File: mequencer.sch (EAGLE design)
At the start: 69 parts, among them IC1 NE555D, IC10 LF353D, IC11 NE555D, IC12 NE555D, IC2 4163D, IC3 74HC85D, IC4 4051D, IC5 4051D, IC6 74HCT04D, IC7 4051D, IC8 4051D, IC9 LF353D, U1 74LVC1G08SE-7

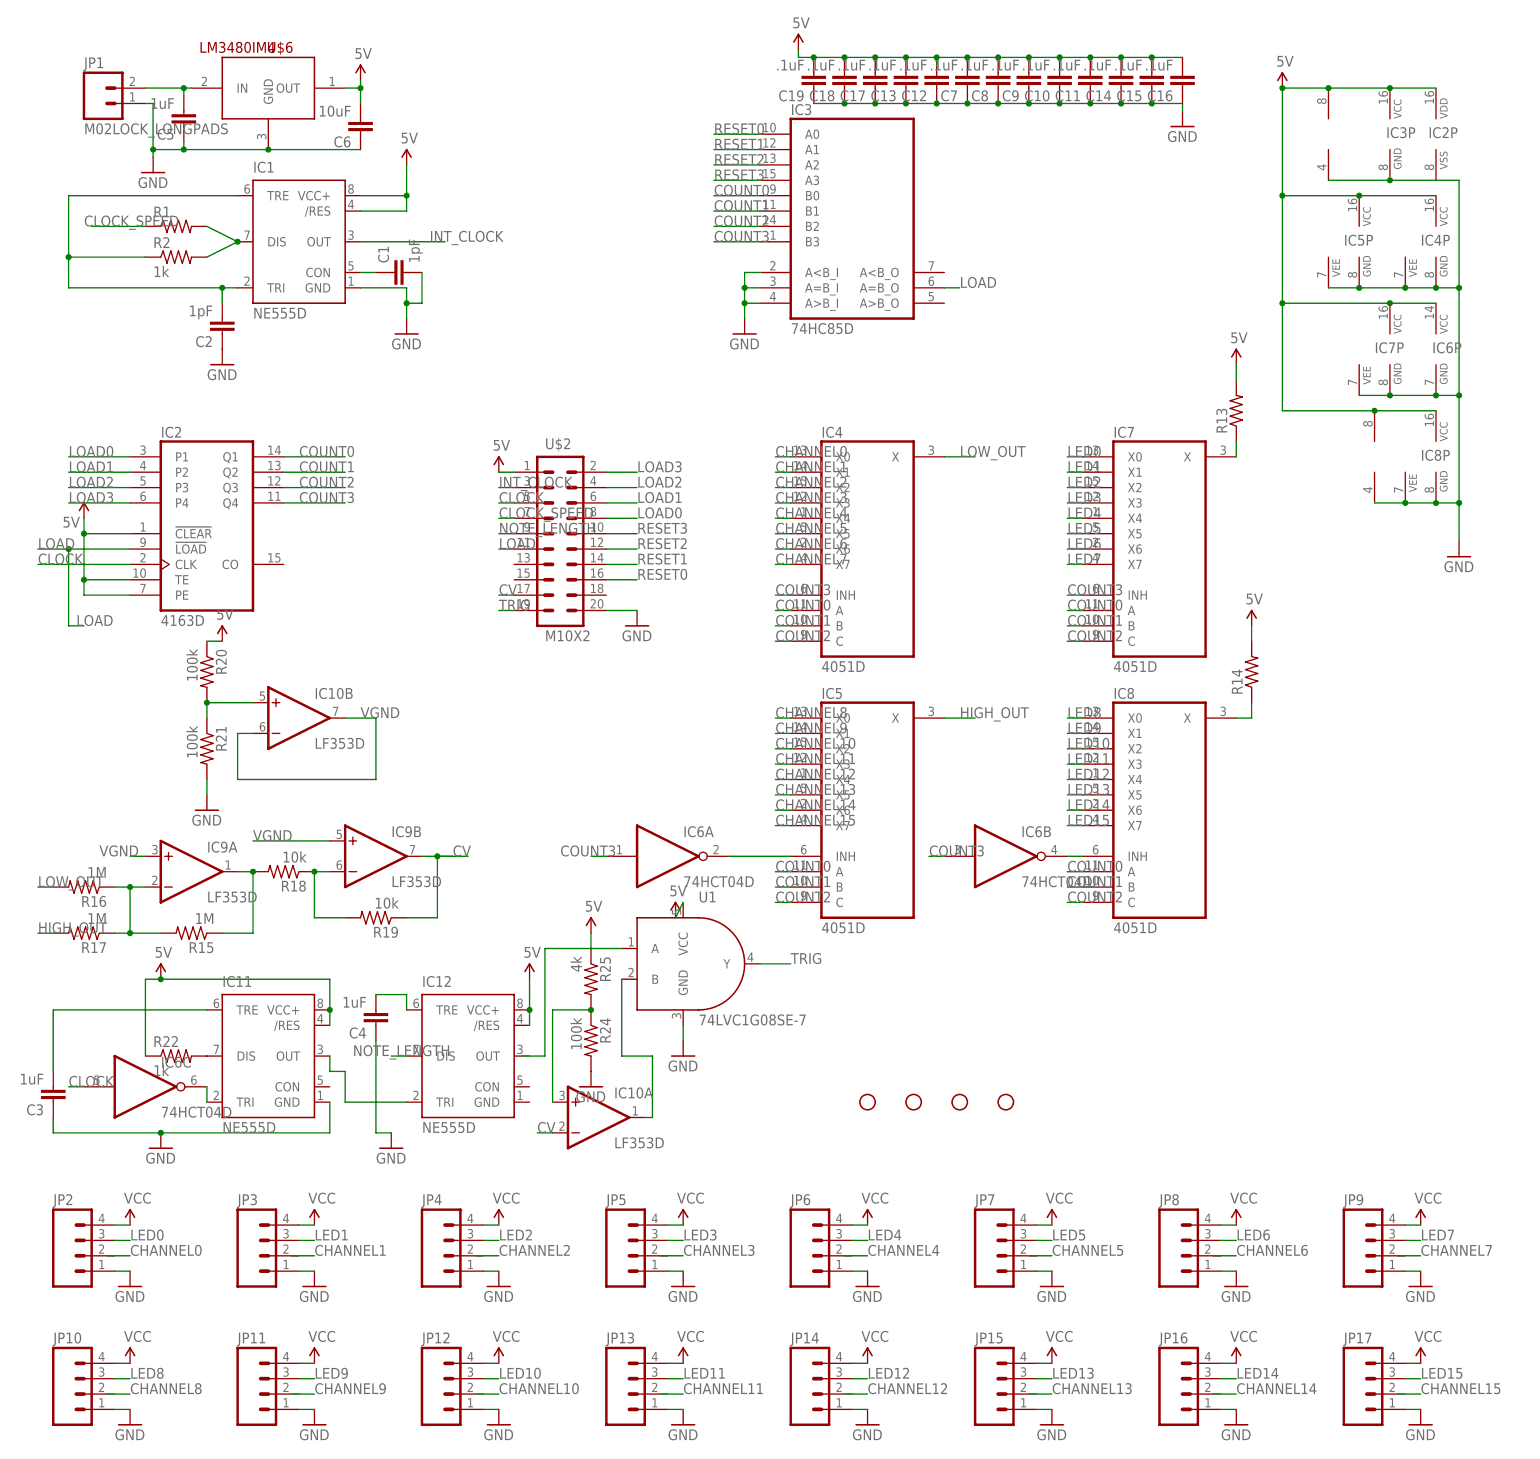
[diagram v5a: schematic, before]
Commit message: test points and jack resistors
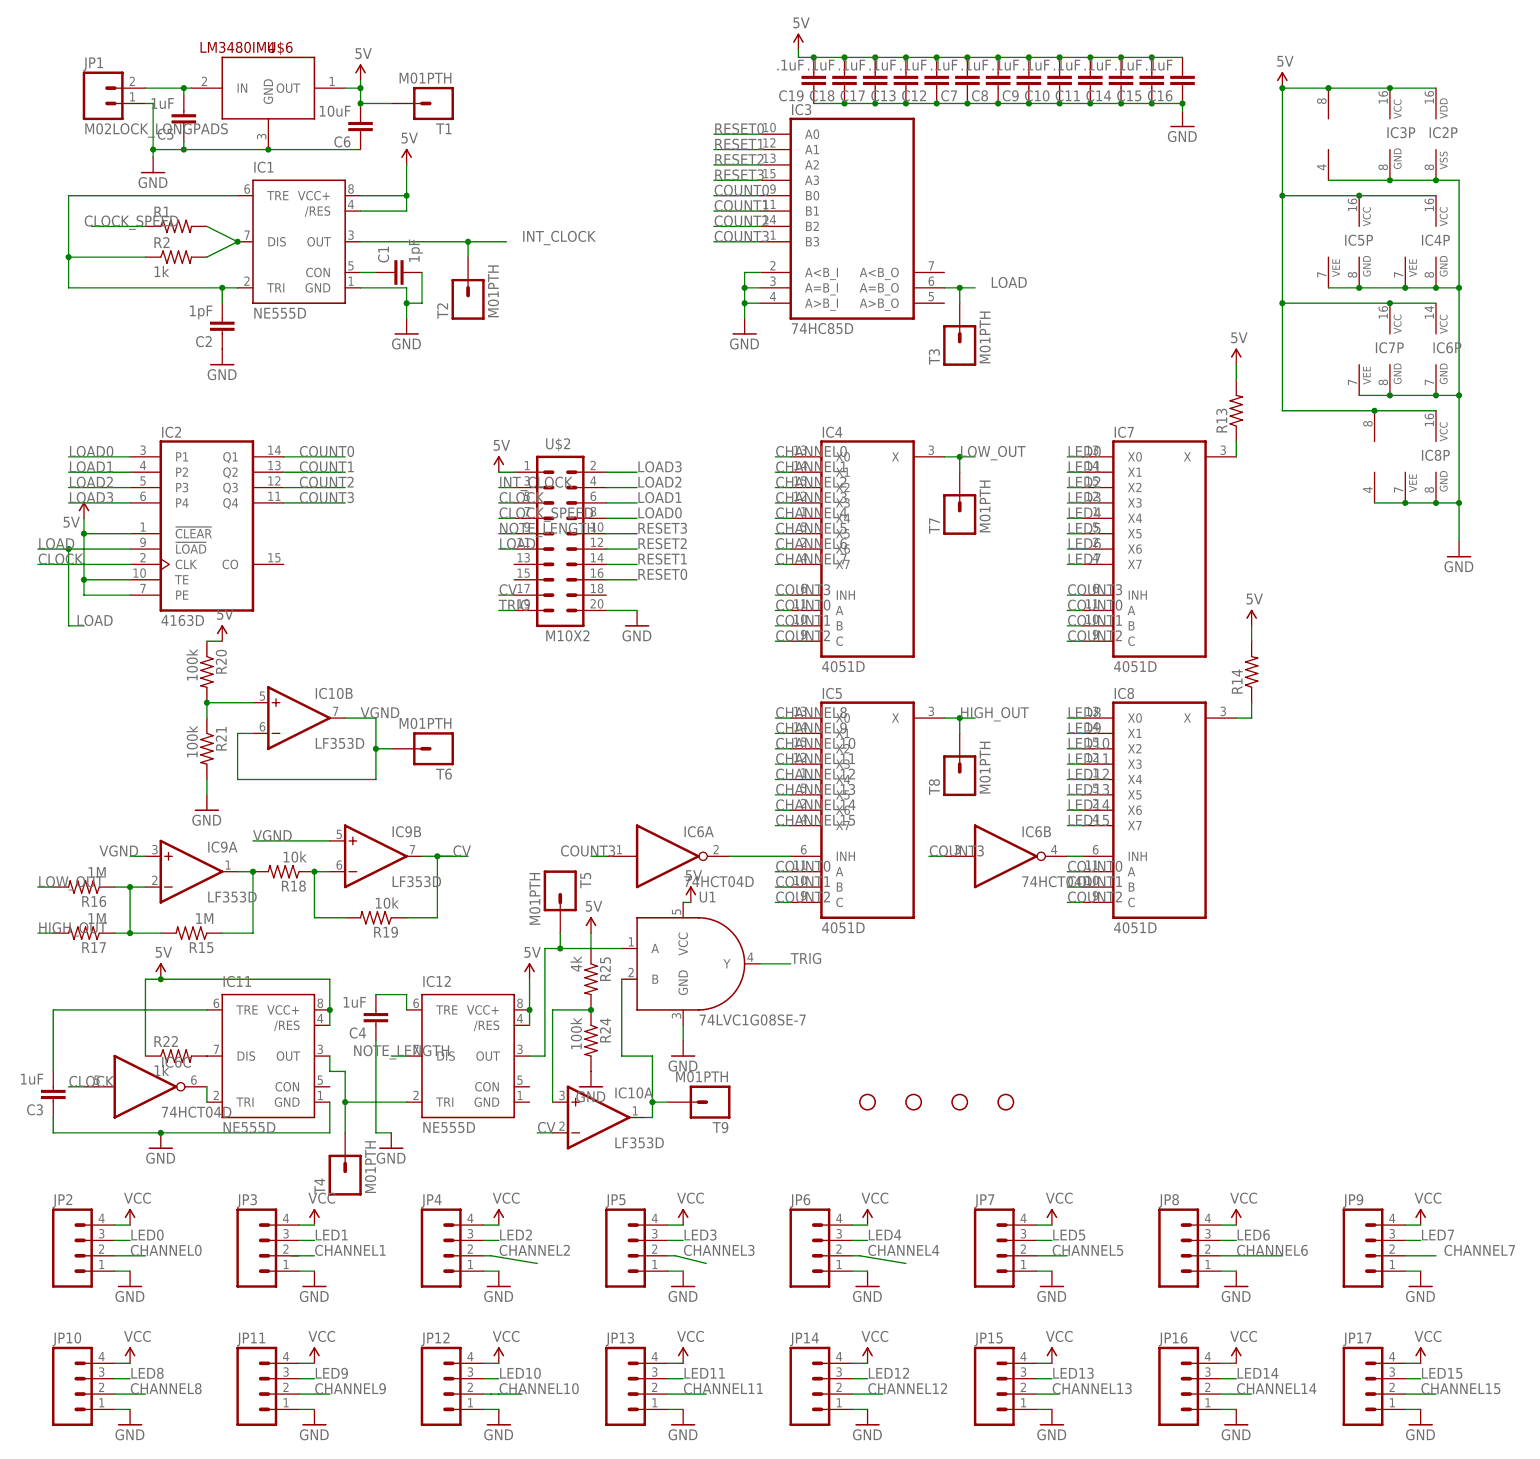
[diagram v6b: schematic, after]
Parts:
- added T1, T2, T3, T4, T5, T6, T7, T8, T9: M01PTH, SparkFun-Connectors:M01PTH
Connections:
- net 5V: now also C12.2, T1.1
- net CHANNEL0: now also JP2.2
- net CHANNEL10: now also JP12.2
- net CHANNEL11: now also JP13.2
- net CHANNEL12: now also JP14.2
- net CHANNEL13: now also JP15.2
- net CHANNEL14: now also JP16.2
- net CHANNEL15: now also JP17.2
- net CHANNEL2: now also JP4.2
- net CHANNEL3: now also JP5.2
- net CHANNEL4: now also JP6.2
- net CHANNEL5: now also JP7.2
- net CHANNEL6: now also JP8.2
- net CHANNEL7: now also JP9.2
- net CHANNEL8: now also JP10.2
- net CHANNEL9: now also JP11.2
- net GND: now also IC2P.VSS
- net HIGH_OUT: now also T8.1
- net INT_CLOCK: now also T2.1
- net LOAD: now also T3.1
- net LOW_OUT: now also T7.1
- net N$22: now also T9.1
- net N$23: now also T4.1
- net N$25: now also IC12.OUT, T5.1
- net VGND: now also T6.1
